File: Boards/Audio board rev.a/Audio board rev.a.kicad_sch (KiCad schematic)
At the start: 104 parts, among them J1 CEC card edge connector large, U1 6821, U10 LM324, U11 MC1458, U2 LM339, U3 LM339, U4 ULN2003A, U5 DAC-08, U6 DAC-08, U7 AH5012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

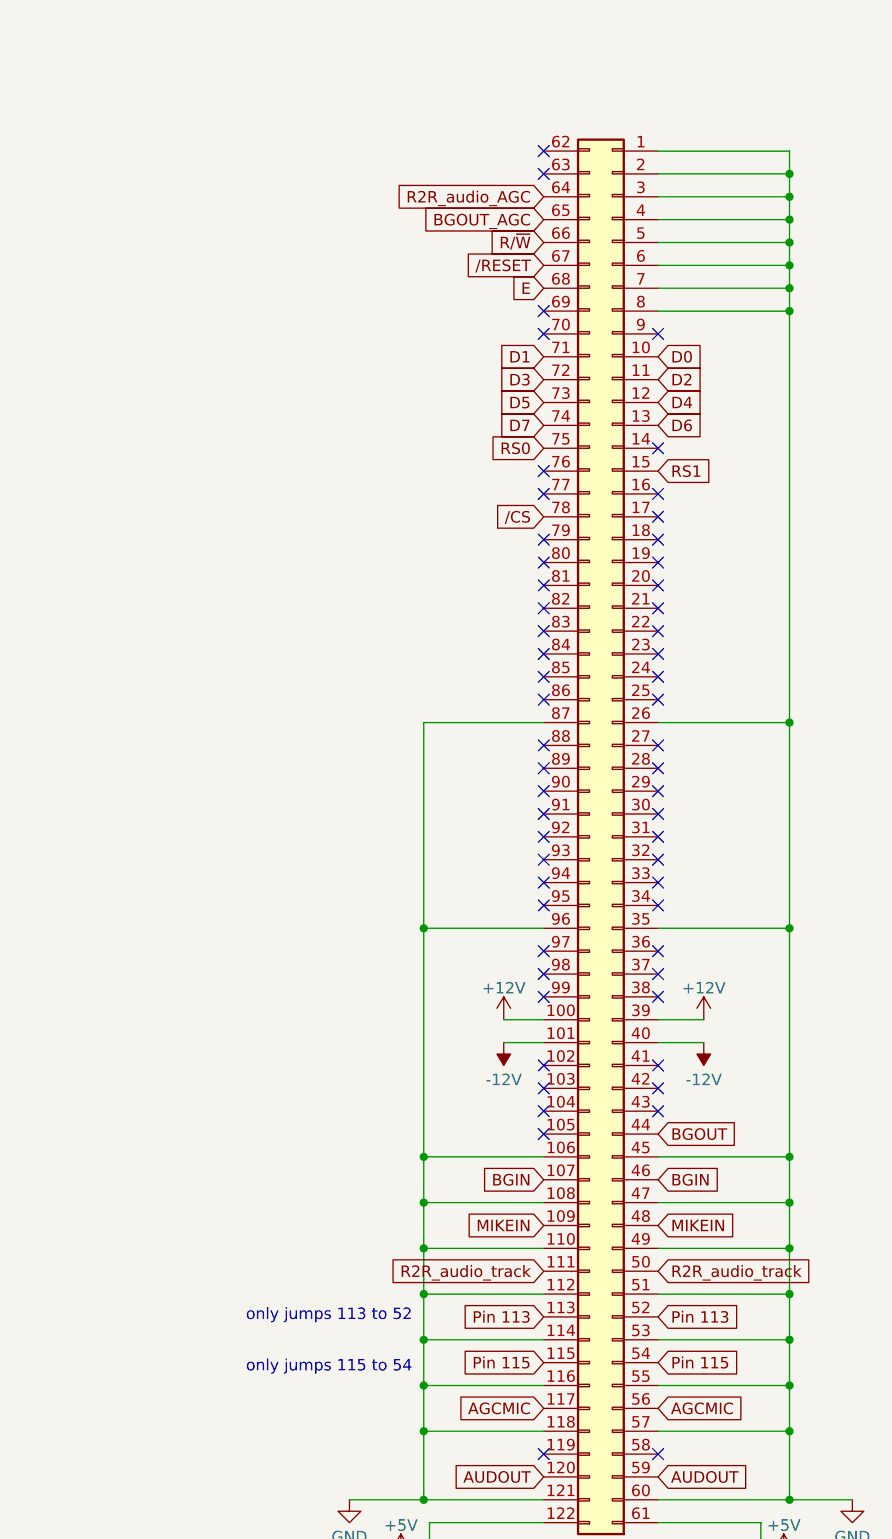
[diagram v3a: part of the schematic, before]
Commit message: revised all net names to reflect new information about 4 channel audio system
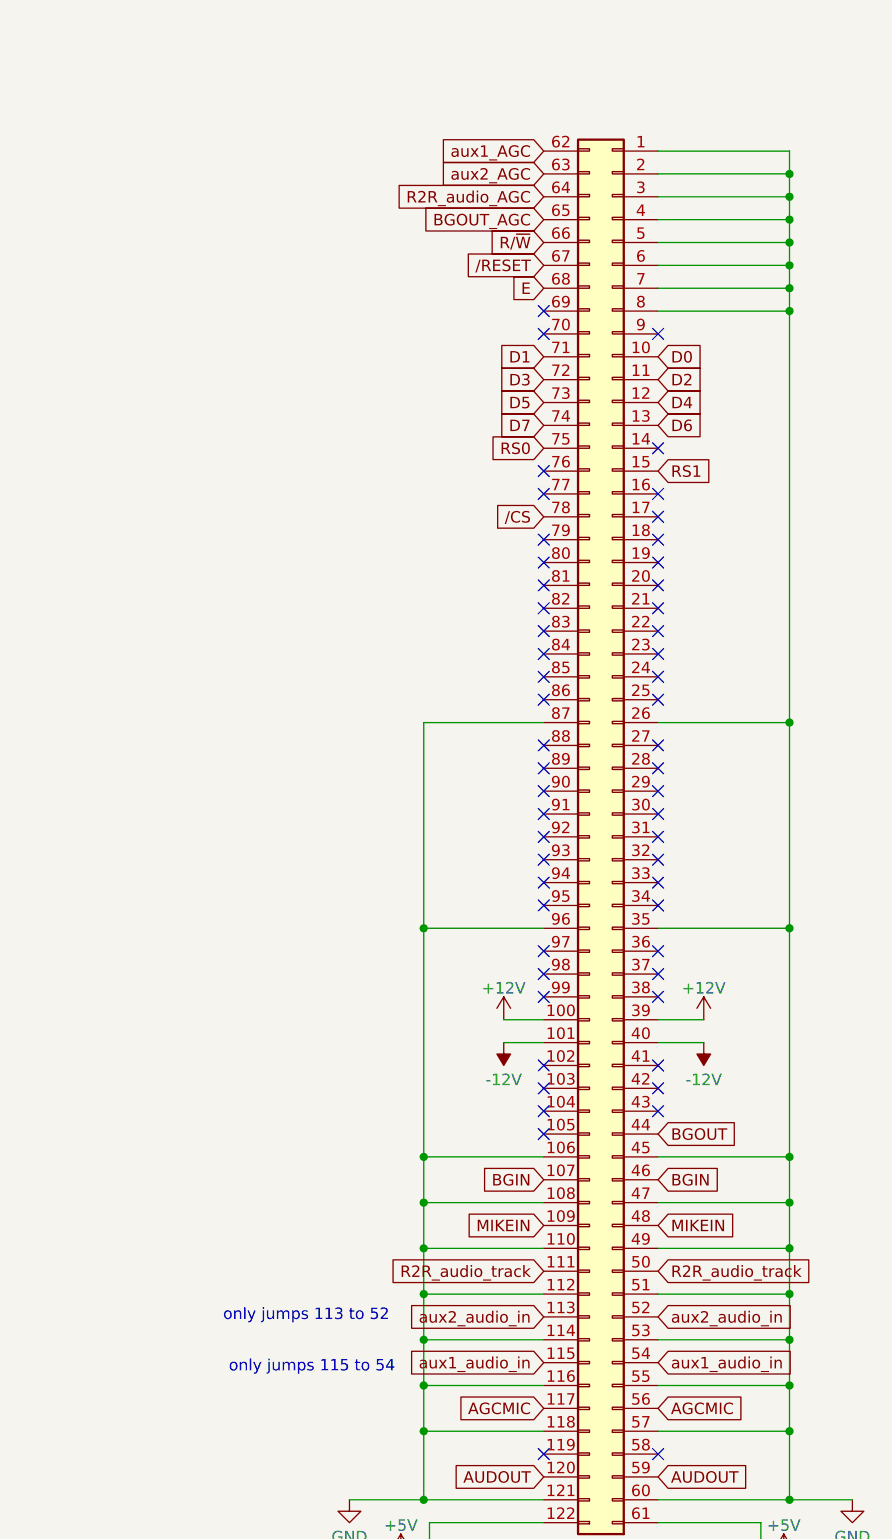
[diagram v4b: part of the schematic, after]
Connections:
- net aux1_AGC: now reaches J1.62 (Pin_62)
- net aux2_AGC: now reaches J1.63 (Pin_63)
- net Pin 113 renamed aux2_audio_in
- net Pin 115 renamed aux1_audio_in
- no-connect marks 69 -> 67
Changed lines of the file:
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@@
   (no_connect (at 267.335 106.68))
   (no_connect (at 494.665 62.865))
-  (no_connect (at 481.965 32.385))
   (no_connect (at 481.965 174.625))
   (no_connect (at 143.51 277.495))
@@
   (no_connect (at 481.965 67.945))
   (no_connect (at 481.965 131.445))
-  (no_connect (at 481.965 29.845))
   (no_connect (at 143.51 264.795))
   (no_connect (at 494.665 133.985))
@@
     (effects (font (size 1.27 1.27)) (justify right bottom))
   )
-  (text "only jumps 115 to 54" (at 467.36 165.735 0)
+  (text "only jumps 115 to 54" (at 465.455 165.735 0)
     (effects (font (size 1.27 1.27)) (justify right bottom))
   )
@@
     (effects (font (size 1.27 1.27)) (justify right bottom))
   )
-  (text "only jumps 113 to 52" (at 467.36 160.02 0)
+  (text "only jumps 113 to 52" (at 464.82 160.02 0)
     (effects (font (size 1.27 1.27)) (justify right bottom))
   )
@@
     )
   )
-  (global_label "Pin 115" (shape input) (at 481.965 164.465 180) (fields_autoplaced)
-    (effects (font (size 1.27 1.27)) (justify right))
-    (property "Intersheetrefs" "${INTERSHEET_REFS}" (at 471.4393 164.465 0)
+  (global_label "aux1_audio_in" (shape input) (at 481.965 164.465 180) (fields_autoplaced)
+    (effects (font (size 1.27 1.27)) (justify right))
+    (property "Intersheetrefs" "${INTERSHEET_REFS}" (at 465.6338 164.465 0)
       (effects (font (size 1.27 1.27)) (justify right) hide)
     )
@@
     )
   )
-  (global_label "Pin 113" (shape input) (at 481.965 159.385 180) (fields_autoplaced)
-    (effects (font (size 1.27 1.27)) (justify right))
-    (property "Intersheetrefs" "${INTERSHEET_REFS}" (at 471.4393 159.385 0)
+  (global_label "aux2_audio_in" (shape input) (at 481.965 159.385 180) (fields_autoplaced)
+    (effects (font (size 1.27 1.27)) (justify right))
+    (property "Intersheetrefs" "${INTERSHEET_REFS}" (at 465.6338 159.385 0)
       (effects (font (size 1.27 1.27)) (justify right) hide)
     )
@@
     )
   )
+  (global_label "aux1_AGC" (shape input) (at 481.965 29.845 180) (fields_autoplaced)
+    (effects (font (size 1.27 1.27)) (justify right))
+    (property "Intersheetrefs" "${INTERSHEET_REFS}" (at 469.9274 29.845 0)
+      (effects (font (size 1.27 1.27)) (justify right) hide)
+    )
+  )
   (global_label "BGOUT" (shape input) (at 197.485 215.265 0) (fields_autoplaced)
     (effects (font (size 1.27 1.27)) (justify left))
@@
     )
   )
-  (global_label "Pin 115" (shape input) (at 494.665 164.465 0) (fields_autoplaced)
-    (effects (font (size 1.27 1.27)) (justify left))
-    (property "Intersheetrefs" "${INTERSHEET_REFS}" (at 505.1907 164.465 0)
+  (global_label "aux1_audio_in" (shape input) (at 494.665 164.465 0) (fields_autoplaced)
+    (effects (font (size 1.27 1.27)) (justify left))
+    (property "Intersheetrefs" "${INTERSHEET_REFS}" (at 510.9962 164.465 0)
       (effects (font (size 1.27 1.27)) (justify left) hide)
     )
@@
     )
   )
+  (global_label "aux2_AGC" (shape input) (at 481.965 32.385 180) (fields_autoplaced)
+    (effects (font (size 1.27 1.27)) (justify right))
+    (property "Intersheetrefs" "${INTERSHEET_REFS}" (at 469.9274 32.385 0)
+      (effects (font (size 1.27 1.27)) (justify right) hide)
+    )
+  )
   (global_label "D4" (shape input) (at 494.665 57.785 0) (fields_autoplaced)
     (effects (font (size 1.27 1.27)) (justify left))
@@
     )
   )
-  (global_label "Pin 113" (shape input) (at 494.665 159.385 0) (fields_autoplaced)
-    (effects (font (size 1.27 1.27)) (justify left))
-    (property "Intersheetrefs" "${INTERSHEET_REFS}" (at 505.1907 159.385 0)
-      (effects (font (size 1.27 1.27)) (justify left) hide)
-    )
+  (global_label "aux2_audio_in" (shape input) (at 494.665 159.385 0) (fields_autoplaced)
+    (effects (font (size 1.27 1.27)) (justify left))
+    (property "Intersheetrefs" "${INTERSHEET_REFS}" (at 510.9962 159.385 0)
+      (effects (font (size 1.27 1.27)) (justify left) hide)
+    )
